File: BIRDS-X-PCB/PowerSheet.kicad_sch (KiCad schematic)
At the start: 11 parts, among them Q201 SI1470DH, Q202 SI1470DH, U201 LTC4361-2, U202 LTC4361-2

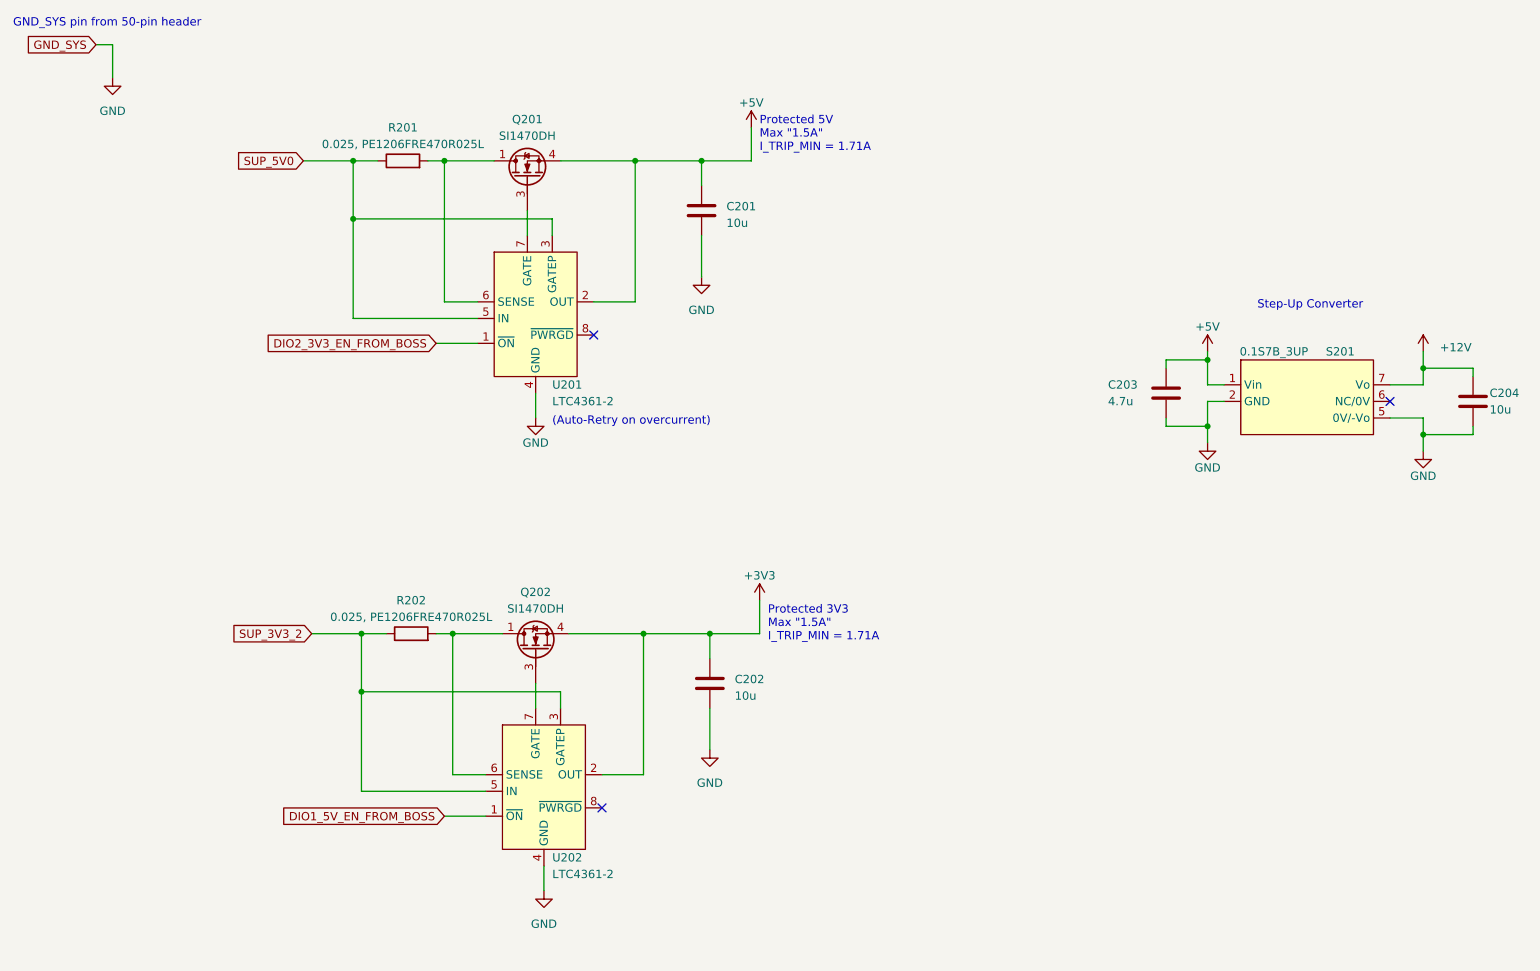
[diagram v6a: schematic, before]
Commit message: Fix power enable issue
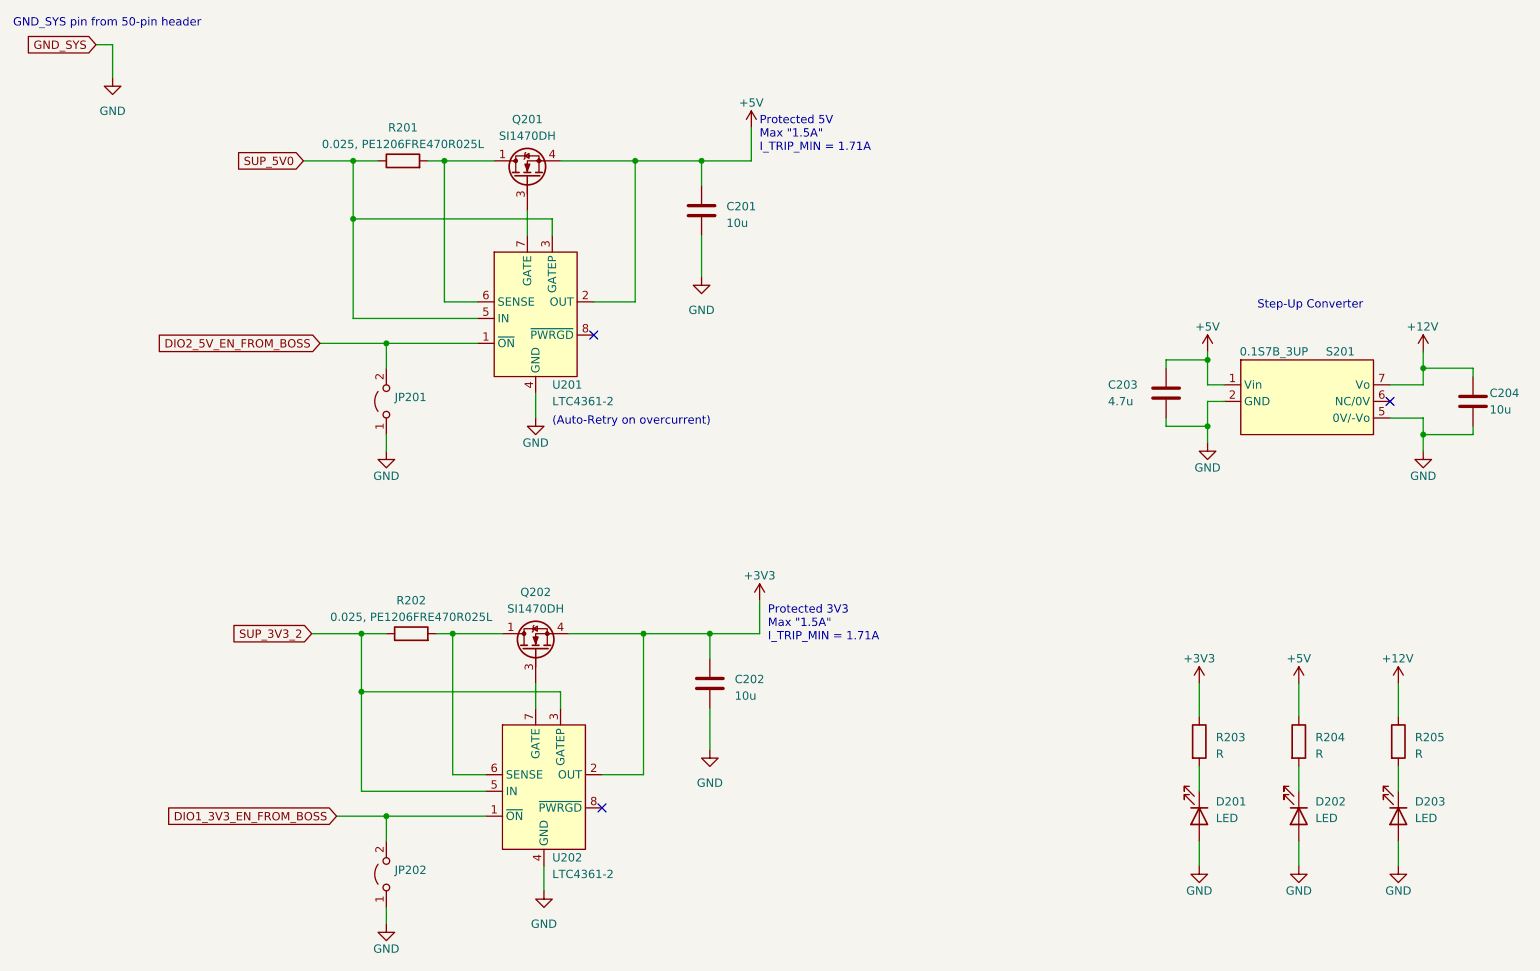
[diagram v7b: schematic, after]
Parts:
- added D201, D202, D203: LED, symbol Device:LED
- added JP201, JP202: Jumper_2_Open, Jumper:SolderJumper-2_P1.3mm_Open_RoundedPad1.0x1.5mm, symbol Jumper:Jumper_2_Open
- added R203, R204, R205: R, Resistor_SMD:R_1206_3216Metric_Pad1.30x1.75mm_HandSolder, symbol Device:R
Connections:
- net +12V: now also R205.1
- net +3V3: now also R203.1
- net +5V: now also R204.1
- net GND: now also D201.2 (A), D202.2 (A), D203.2 (A), JP201.1 (A), JP202.1 (A)
- net DIO1_5V_EN_FROM_BOSS renamed DIO1_3V3_EN_FROM_BOSS
- net DIO1_3V3_EN_FROM_BOSS: now also JP202.2 (B)
- net DIO2_3V3_EN_FROM_BOSS renamed DIO2_5V_EN_FROM_BOSS
- net DIO2_5V_EN_FROM_BOSS: now also JP201.2 (B)
- new net: D202.1 (K), R204.2
- new net: D201.1 (K), R203.2
- new net: D203.1 (K), R205.2

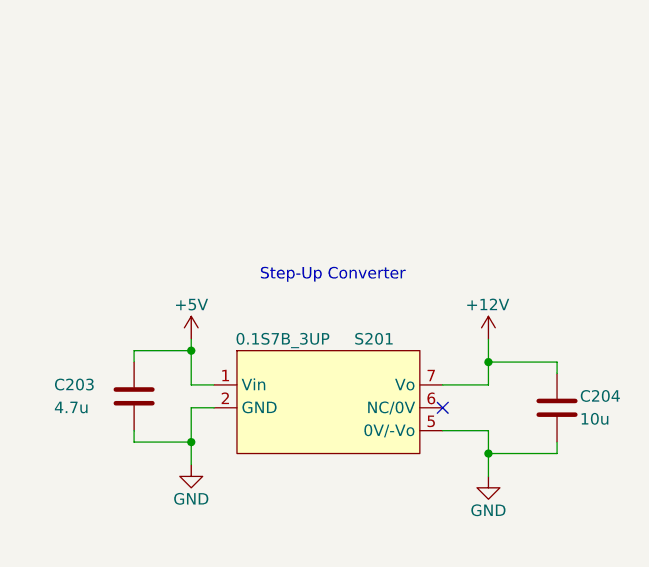
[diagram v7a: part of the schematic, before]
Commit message: Add footprints
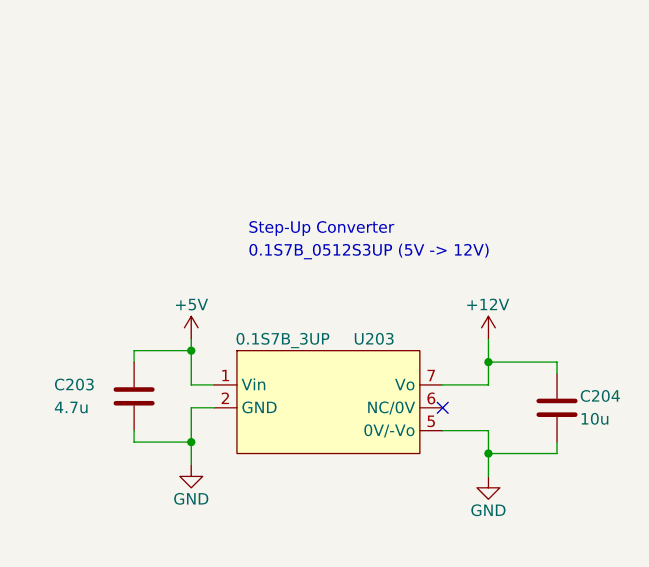
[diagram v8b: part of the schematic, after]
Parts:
- D201, D202, D203: footprint (none) -> LED_SMD:LED_1206_3216Metric_Pad1.42x1.75mm_HandSolder
- U203: renamed from S201; footprint (none) -> BIRDS-X_Footprints_Lib:Converter_DCDC_Gaptec_0.1S7B_3UP_THT
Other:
- note added: "0.1S7B_0512S3UP (5V -> 12V)"
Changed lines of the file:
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@@
     (effects (font (size 1.27 1.27)) (justify left bottom))
   )
-  (text "Step-Up Converter" (at 207.01 64.77 0)
+  (text "Step-Up Converter" (at 205.74 59.69 0)
     (effects (font (size 1.27 1.27)) (justify left bottom))
   )
   (text "Protected 5V\nMax \"1.5A\"\nI_TRIP_MIN = 1.71A" (at 130.81 40.64 0)
+    (effects (font (size 1.27 1.27)) (justify left bottom))
+  )
+  (text "0.1S7B_0512S3UP (5V -> 12V)" (at 205.74 62.23 0)
     (effects (font (size 1.27 1.27)) (justify left bottom))
   )
@@
       (effects (font (size 1.27 1.27)) (justify left))
     )
-    (property "Footprint" "" (at 213.36 142.24 0)
+    (property "Footprint" "LED_SMD:LED_1206_3216Metric_Pad1.42x1.75mm_HandSolder" (at 213.36 142.24 0)
       (effects (font (size 1.27 1.27)) hide)
     )
@@
       (effects (font (size 1.27 1.27)) (justify left))
     )
-    (property "Footprint" "" (at 198.12 142.24 0)
+    (property "Footprint" "LED_SMD:LED_1206_3216Metric_Pad1.42x1.75mm_HandSolder" (at 198.12 142.24 0)
       (effects (font (size 1.27 1.27)) hide)
     )
@@
       (effects (font (size 1.27 1.27)) (justify left))
     )
-    (property "Footprint" "" (at 228.6 142.24 0)
+    (property "Footprint" "LED_SMD:LED_1206_3216Metric_Pad1.42x1.75mm_HandSolder" (at 228.6 142.24 0)
       (effects (font (size 1.27 1.27)) hide)
     )
@@
   (symbol (lib_id "BIRDS-X_Symbols_Lib:0.1S7B_3UP") (at 209.55 78.74 0) (unit 1)
     (in_bom yes) (on_board yes) (dnp no)
-    (property "Reference" "S201" (at 219.71 71.12 0)
+    (property "Reference" "U203" (at 219.71 71.12 0)
       (effects (font (size 1.27 1.27)))
     )
@@
       (effects (font (size 1.27 1.27)))
     )
-    (property "Footprint" "" (at 207.01 78.74 90)
+    (property "Footprint" "BIRDS-X_Footprints_Lib:Converter_DCDC_Gaptec_0.1S7B_3UP_THT" (at 207.01 78.74 90)
       (effects (font (size 1.27 1.27)) hide)
     )
@@
       (project "BIRDS-X-PCB"
         (path "/c2796b15-795a-4d6e-ad4b-0ba87ded4bc9/f0b1214b-f453-423f-b2cf-f5d10e08eafe"
-          (reference "S201") (unit 1)
-        )
-      )
+          (reference "U203") (unit 1)
+        )
+      )
